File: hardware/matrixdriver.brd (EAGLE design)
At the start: 50 x 50 mm, 35 parts, among them IC1 75176AD, IC2 4017D, IC3 ULN2803, IC4 7805DT, Q1 20MHZ, Q2 MMBT4403LT1SMD, Q3 MMBT4403LT1SMD, Q4 MMBT4403LT1SMD, Q5 MMBT4403LT1SMD, Q6 MMBT4403LT1SMD, Q7 MMBT4403LT1SMD, Q8 MMBT4403LT1SMD, Q9 MMBT4403LT1SMD

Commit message: Release Candidate
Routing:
- net N$16: track 41.9 -> 43.3 mm
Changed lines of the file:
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@@
 <grid distance="12.5" unitdist="mil" unit="mm" style="lines" multiple="25" display="no" altdistance="25" altunitdist="mil" altunit="mm"/>
 <layers>
-<layer number="1" name="Top" color="4" fill="1" visible="no" active="yes"/>
-<layer number="16" name="Bottom" color="1" fill="1" visible="no" active="yes"/>
+<layer number="1" name="Top" color="4" fill="1" visible="yes" active="yes"/>
+<layer number="16" name="Bottom" color="1" fill="1" visible="yes" active="yes"/>
 <layer number="17" name="Pads" color="2" fill="1" visible="yes" active="yes"/>
 <layer number="18" name="Vias" color="2" fill="1" visible="yes" active="yes"/>
 <layer number="19" name="Unrouted" color="6" fill="1" visible="yes" active="yes"/>
-<layer number="20" name="Dimension" color="15" fill="1" visible="no" active="yes"/>
+<layer number="20" name="Dimension" color="15" fill="1" visible="yes" active="yes"/>
 <layer number="21" name="tPlace" color="7" fill="1" visible="no" active="yes"/>
-<layer number="22" name="bPlace" color="7" fill="1" visible="yes" active="yes"/>
+<layer number="22" name="bPlace" color="7" fill="1" visible="no" active="yes"/>
 <layer number="23" name="tOrigins" color="15" fill="1" visible="yes" active="yes"/>
 <layer number="24" name="bOrigins" color="15" fill="1" visible="yes" active="yes"/>
 <layer number="25" name="tNames" color="7" fill="1" visible="yes" active="yes"/>
-<layer number="26" name="bNames" color="7" fill="1" visible="yes" active="yes"/>
-<layer number="27" name="tValues" color="7" fill="1" visible="yes" active="yes"/>
+<layer number="26" name="bNames" color="7" fill="1" visible="no" active="yes"/>
+<layer number="27" name="tValues" color="7" fill="1" visible="no" active="yes"/>
 <layer number="28" name="bValues" color="7" fill="1" visible="no" active="yes"/>
 <layer number="29" name="tStop" color="7" fill="3" visible="yes" active="yes"/>
@@
 <layer number="33" name="tFinish" color="6" fill="3" visible="yes" active="yes"/>
 <layer number="34" name="bFinish" color="6" fill="6" visible="yes" active="yes"/>
-<layer number="35" name="tGlue" color="7" fill="4" visible="no" active="yes"/>
-<layer number="36" name="bGlue" color="7" fill="5" visible="no" active="yes"/>
+<layer number="35" name="tGlue" color="7" fill="4" visible="yes" active="yes"/>
+<layer number="36" name="bGlue" color="7" fill="5" visible="yes" active="yes"/>
 <layer number="37" name="tTest" color="7" fill="1" visible="yes" active="yes"/>
 <layer number="38" name="bTest" color="7" fill="1" visible="yes" active="yes"/>
@@
 <layer number="98" name="Guide" color="6" fill="1" visible="no" active="no"/>
 <layer number="100" name="Muster" color="7" fill="1" visible="no" active="no"/>
-<layer number="101" name="Patch_Top" color="12" fill="4" visible="yes" active="yes"/>
+<layer number="101" name="Patch_Top" color="12" fill="4" visible="no" active="yes"/>
 <layer number="102" name="Vscore" color="7" fill="1" visible="no" active="yes"/>
 <layer number="103" name="fp3" color="7" fill="1" visible="no" active="yes"/>
-<layer number="104" name="Name" color="7" fill="1" visible="yes" active="yes"/>
+<layer number="104" name="Name" color="7" fill="1" visible="no" active="yes"/>
 <layer number="105" name="Beschreib" color="9" fill="1" visible="no" active="yes"/>
-<layer number="106" name="BGA-Top" color="4" fill="1" visible="yes" active="yes"/>
-<layer number="107" name="BD-Top" color="5" fill="1" visible="yes" active="yes"/>
+<layer number="106" name="BGA-Top" color="4" fill="1" visible="no" active="yes"/>
+<layer number="107" name="BD-Top" color="5" fill="1" visible="no" active="yes"/>
 <layer number="108" name="fp8" color="7" fill="1" visible="no" active="yes"/>
 <layer number="109" name="fp9" color="7" fill="1" visible="no" active="yes"/>
@@
 <layer number="111" name="LPC17xx" color="7" fill="1" visible="yes" active="yes"/>
 <layer number="112" name="tSilk" color="7" fill="1" visible="yes" active="yes"/>
-<layer number="116" name="Patch_BOT" color="9" fill="4" visible="yes" active="yes"/>
+<layer number="116" name="Patch_BOT" color="9" fill="4" visible="no" active="yes"/>
 <layer number="121" name="_tsilk" color="7" fill="1" visible="yes" active="yes"/>
 <layer number="122" name="_bsilk" color="7" fill="1" visible="yes" active="yes"/>
@@
 <wire x1="50" y1="50" x2="0" y2="50" width="0" layer="20"/>
 <wire x1="0" y1="50" x2="0" y2="0" width="0" layer="20"/>
-<text x="2.2225" y="48.26" size="1.016" layer="1" font="vector" rot="R270">dirarare
+<text x="2.8575" y="46.355" size="1.016" layer="1" font="vector" rot="R270">dirarare
 Matrixdriver</text>
-<text x="46.6725" y="7.9375" size="1.016" layer="1" font="vector" rot="R270">REV 1</text>
-<hole x="2.5" y="48" drill="1.1"/>
-<hole x="48" y="2.5" drill="1.1"/>
-<hole x="48" y="48" drill="1.1"/>
+<text x="48.26" y="9.525" size="1.016" layer="1" font="vector" rot="R270">REV 1</text>
+<hole x="2.5" y="47.5" drill="1.1"/>
+<hole x="47.5" y="2.5" drill="1.1"/>
+<hole x="47.5" y="47.5" drill="1.1"/>
 <hole x="2.5" y="2.5" drill="1.1"/>
 </plain>
@@
 <contactref element="C4" pad="2"/>
 <contactref element="IC2" pad="8"/>
-<via x="5.715" y="39.37" extent="1-16" drill="0.6"/>
+<via x="6.6675" y="39.37" extent="1-16" drill="0.6"/>
 <via x="21.59" y="27.305" extent="1-16" drill="0.6"/>
 <via x="19.685" y="10.4775" extent="1-16" drill="0.6"/>
@@
 <vertex x="0.3175" y="0.9525"/>
 <vertex x="0.9525" y="0.3175"/>
-<vertex x="49.53" y="0.3175"/>
-<vertex x="49.2125" y="0.9525"/>
+<vertex x="49.8475" y="0.3175"/>
 <vertex x="49.8475" y="49.8475"/>
 </polygon>
@@
 <wire x1="33.02" y1="20.32" x2="33.655" y2="19.685" width="0.4064" layer="1"/>
 <via x="33.655" y="19.685" extent="1-16" drill="0.6"/>
-<wire x1="33.655" y1="19.685" x2="33.02" y2="20.32" width="0.4064" layer="16"/>
-<wire x1="33.02" y1="20.32" x2="22.225" y2="20.32" width="0.4064" layer="16"/>
-<wire x1="22.225" y1="20.32" x2="21.59" y2="20.955" width="0.4064" layer="16"/>
+<wire x1="33.655" y1="19.685" x2="33.02" y2="19.05" width="0.4064" layer="16"/>
+<wire x1="33.02" y1="19.05" x2="21.9075" y2="19.05" width="0.4064" layer="16"/>
+<wire x1="21.9075" y1="19.05" x2="21.59" y2="19.3675" width="0.4064" layer="16"/>
+<wire x1="21.59" y1="19.3675" x2="21.59" y2="20.955" width="0.4064" layer="16"/>
 <via x="21.59" y="20.955" extent="1-16" drill="0.6" shape="octagon"/>
 <wire x1="21.59" y1="20.955" x2="21.59" y2="19.05" width="0.4064" layer="1"/>

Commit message: REV.1 Finalisation
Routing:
- net N$65: vias 1 -> 2
- net N$62: vias 0 -> 1
- net N$61: vias 0 -> 1
- net N$60: vias 2 -> 1
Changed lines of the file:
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@@
 <via x="24.13" y="36.195" extent="1-16" drill="0.6"/>
 <via x="35.56" y="24.13" extent="1-16" drill="0.6"/>
-<via x="19.05" y="20.955" extent="1-16" drill="0.6" shape="octagon"/>
+<via x="19.05" y="20.955" extent="1-16" drill="0.6"/>
 <contactref element="C5" pad="1"/>
 <via x="3.81" y="25.4" extent="1-16" drill="0.6"/>
@@
 <wire x1="21.9075" y1="19.05" x2="21.59" y2="19.3675" width="0.4064" layer="16"/>
 <wire x1="21.59" y1="19.3675" x2="21.59" y2="20.955" width="0.4064" layer="16"/>
-<via x="21.59" y="20.955" extent="1-16" drill="0.6" shape="octagon"/>
+<via x="21.59" y="20.955" extent="1-16" drill="0.6"/>
 <wire x1="21.59" y1="20.955" x2="21.59" y2="19.05" width="0.4064" layer="1"/>
 <wire x1="21.59" y1="19.05" x2="21.59" y2="18.5166" width="0.4064" layer="1"/>
@@
 <contactref element="JP4" pad="2"/>
 <contactref element="U$1" pad="6"/>
-<wire x1="22.225" y1="13.335" x2="19.685" y2="13.335" width="0.4064" layer="1"/>
-<via x="19.685" y="13.335" extent="1-16" drill="0.6" shape="octagon"/>
-<wire x1="19.685" y1="13.335" x2="12.065" y2="13.335" width="0.4064" layer="16"/>
+<wire x1="22.225" y1="13.335" x2="12.065" y2="13.335" width="0.4064" layer="16"/>
 <via x="12.065" y="13.335" extent="1-16" drill="0.6"/>
 <wire x1="12.065" y1="13.335" x2="12.065" y2="11.2395" width="0.4064" layer="1"/>
@@
 <contactref element="JP4" pad="4"/>
 <contactref element="U$1" pad="9"/>
-<wire x1="24.765" y1="13.335" x2="24.765" y2="14.605" width="0.4064" layer="1"/>
-<wire x1="24.765" y1="14.605" x2="24.13" y2="15.24" width="0.4064" layer="1"/>
-<wire x1="24.13" y1="15.24" x2="16.51" y2="15.24" width="0.4064" layer="1"/>
+<wire x1="24.765" y1="13.335" x2="24.765" y2="14.605" width="0.4064" layer="16"/>
+<wire x1="24.765" y1="14.605" x2="24.13" y2="15.24" width="0.4064" layer="16"/>
+<wire x1="24.13" y1="15.24" x2="16.51" y2="15.24" width="0.4064" layer="16"/>
 <wire x1="16.51" y1="15.24" x2="15.875" y2="14.605" width="0.4064" layer="1"/>
 <wire x1="15.875" y1="14.605" x2="15.875" y2="11.2395" width="0.4064" layer="1"/>
+<via x="16.51" y="15.24" extent="1-16" drill="0.6"/>
 </signal>
 <signal name="N$62">
 <contactref element="JP4" pad="6"/>
 <contactref element="U$1" pad="11"/>
-<wire x1="27.305" y1="13.335" x2="27.305" y2="15.24" width="0.4064" layer="1"/>
+<wire x1="27.305" y1="13.335" x2="27.305" y2="15.24" width="0.4064" layer="16"/>
 <wire x1="27.305" y1="15.24" x2="26.67" y2="15.875" width="0.4064" layer="1"/>
 <wire x1="26.67" y1="15.875" x2="18.415" y2="15.875" width="0.4064" layer="1"/>
 <wire x1="18.415" y1="15.875" x2="17.145" y2="16.51" width="0.4064" layer="1"/>
 <wire x1="17.145" y1="16.51" x2="17.145" y2="20.4851" width="0.4064" layer="1"/>
+<via x="27.305" y="15.24" extent="1-16" drill="0.6"/>
 </signal>
 <signal name="N$65">
@@
 <contactref element="U$2" pad="+"/>
 <wire x1="40.18" y1="24.765" x2="40.005" y2="27.94" width="0.4064" layer="16"/>
-<via x="40.005" y="27.94" extent="1-16" drill="0.6" shape="square"/>
+<via x="40.005" y="27.94" extent="1-16" drill="0.6"/>
 <wire x1="40.005" y1="27.94" x2="40.005" y2="28.575" width="0.4064" layer="1"/>
 <wire x1="40.005" y1="28.575" x2="42.545" y2="31.115" width="0.4064" layer="1"/>
 <wire x1="42.545" y1="31.115" x2="42.545" y2="31.75" width="0.4064" layer="1"/>
 <wire x1="42.545" y1="31.75" x2="42.8625" y2="32.0675" width="0.4064" layer="1"/>
-<wire x1="41.91" y1="23.035" x2="40.18" y2="24.765" width="0.4064" layer="1"/>
+<wire x1="41.91" y1="23.035" x2="40.18" y2="24.765" width="0.4064" layer="16"/>
 <wire x1="44.075" y1="32.03" x2="42.9" y2="32.03" width="0.4064" layer="1"/>
 <wire x1="42.9" y1="32.03" x2="42.8625" y2="32.0675" width="0.4064" layer="1"/>
+<via x="41.91" y="23.035" extent="1-16" drill="0.6"/>
 </signal>
 <signal name="N$11">

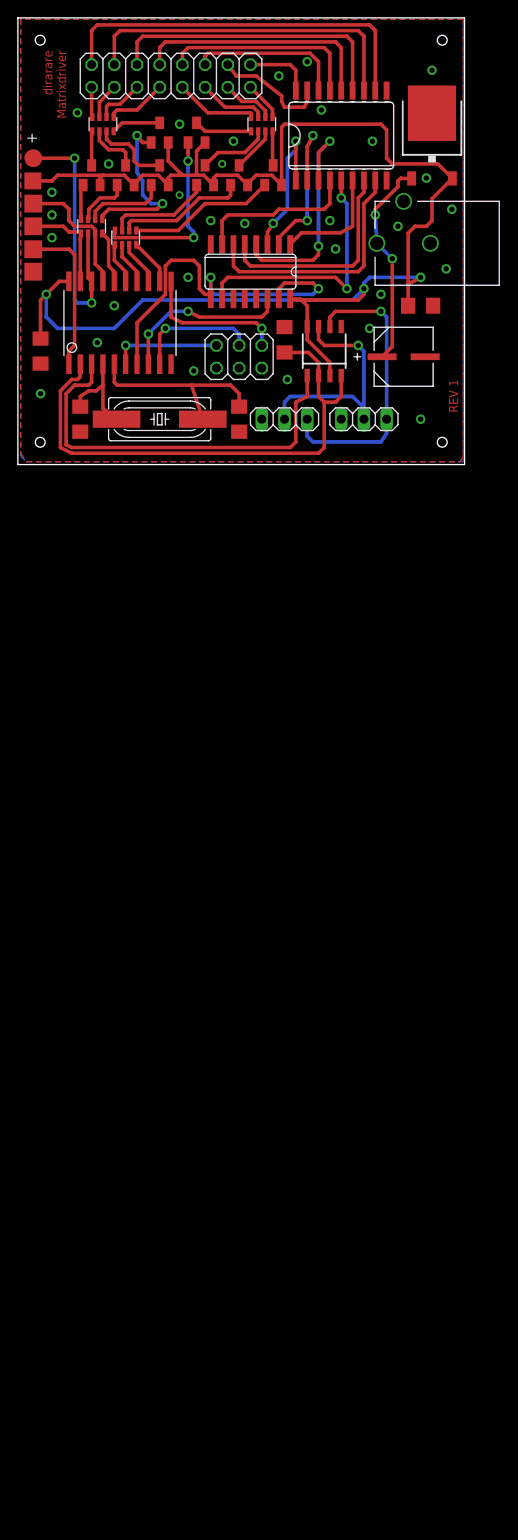
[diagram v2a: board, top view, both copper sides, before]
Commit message: Fix errors behind transistor
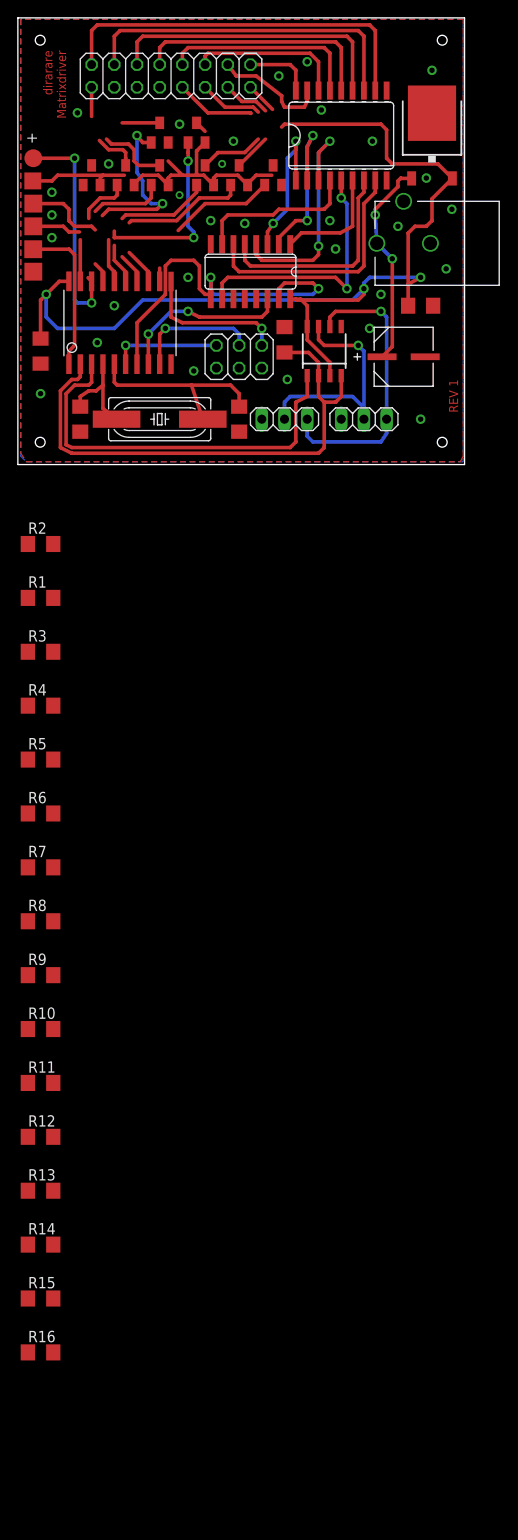
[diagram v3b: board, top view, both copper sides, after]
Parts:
- removed CTS742C083_1, CTS742C083_2: 1k, resistor-net:CTS742C083
- removed CTS742C083_3, CTS742C083_4: 10, resistor-net:CTS742C083
- added R1, R2, R3, R4, R5, R6, R7, R8: 1k, resistor:R1206
- added R10, R11, R12, R13, R14, R15, R16, R9: 10, resistor:R1206
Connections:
- removed net N$34: CTS742C083_3.7, JP1.3
- removed net N$35: CTS742C083_3.6, JP1.5
- removed net N$36: CTS742C083_3.5, JP1.7
- removed net N$56: CTS742C083_3.1, Q2.C
- new net N$44: Q2.E, R9.1
- new net N$45: Q3.E, R10.1
- new net N$46: Q5.E, R12.1
- new net N$461: C4.1, C5.2, IC1.3, IC1.8, IC2.16, IC4.2, Q4.E, Q6.E, Q7.E, Q8.E, R11.1, TP2.TP, U$1.20
- net N$1: now also R5.1; no longer CTS742C083_2.4
- net N$13: now also R16.2; no longer CTS742C083_4.8
- net N$2: now also R6.1; no longer CTS742C083_2.3
- net N$29: now also R15.2; no longer CTS742C083_4.7
- net N$3: now also R7.1; no longer CTS742C083_2.2
- net N$30: now also R14.2; no longer CTS742C083_4.6
- net N$31: now also R13.2; no longer CTS742C083_4.5
- net N$32: now also R3.2; no longer CTS742C083_1.7
- net N$33: now also Q2.C; no longer CTS742C083_3.8
- net N$37: now also R4.2; no longer CTS742C083_1.8
- net N$38: now also R2.2; no longer CTS742C083_1.6
- net N$39: now also R1.2; no longer CTS742C083_1.5
- net N$4: now also R8.1; no longer CTS742C083_2.1
- net N$40: now also R6.2; no longer CTS742C083_2.6
- net N$41: now also R5.2; no longer CTS742C083_2.5
- net N$42: now also R8.2; no longer CTS742C083_2.8
- net N$43: now also R7.2; no longer CTS742C083_2.7
- net N$49: now also R13.1; no longer CTS742C083_4.4
- net N$5: now also R1.1; no longer CTS742C083_1.4
- net N$50: now also R14.1; no longer CTS742C083_4.3
- net N$51: now also R15.1; no longer CTS742C083_4.2
- net N$52: now also R16.1; no longer CTS742C083_4.1
- net N$53: now also JP1.7; no longer CTS742C083_3.4
- net N$54: now also JP1.5; no longer CTS742C083_3.3
- net N$55: now also JP1.3; no longer CTS742C083_3.2
- net N$6: now also R2.1; no longer CTS742C083_1.3
- net N$7: now also R3.1; no longer CTS742C083_1.2
- net N$8: now also R4.1; no longer CTS742C083_1.1
- net VCC: now also R10.2, R12.2, R9.2; no longer C4.1, C5.2, IC1.3, IC1.8, IC2.16, IC4.2, Q2.E, Q3.E, Q4.E, Q5.E, Q6.E, Q7.E, Q8.E, Q9.E, TP2.TP, U$1.20
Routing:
- net VCC: track 167.4 -> 0.00 mm, vias 3 -> 0
- net N$461: track 0.00 -> 154.8 mm, vias 0 -> 3
- net N$36: track 6.76 -> 0.00 mm
- net N$35: track 5.48 -> 0.00 mm
- net N$52: track 6.49 -> 1.34 mm
- net N$7: track 30.5 -> 25.5 mm
- net N$41: track 16.5 -> 11.8 mm
- net N$34: track 4.02 -> 0.00 mm
- net N$56: track 3.84 -> 0.00 mm
- net N$6: track 15.0 -> 11.2 mm
- net N$49: track 3.84 -> 0.10 mm
- net N$1: track 5.17 -> 1.48 mm
- net N$37: track 3.92 -> 0.35 mm
- net N$43: track 11.9 -> 10.6 mm
- net N$3: track 4.78 -> 3.44 mm
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
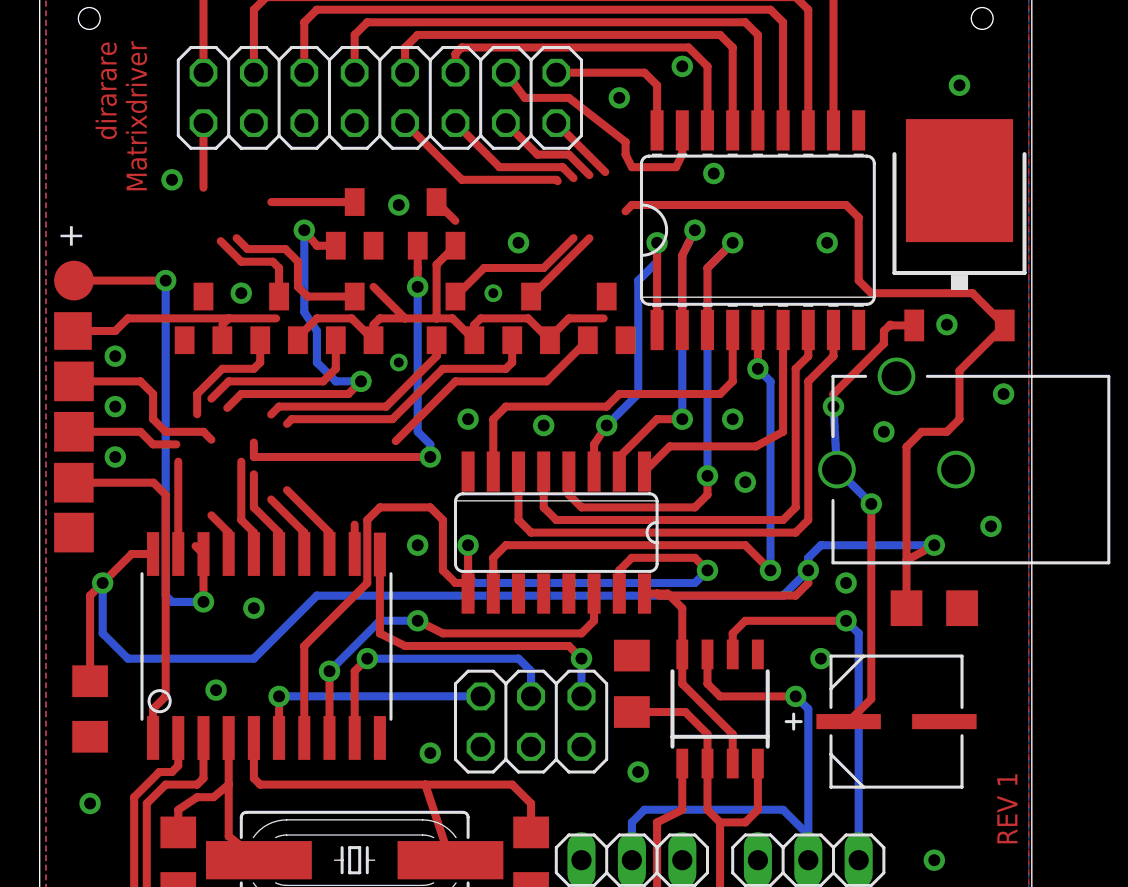
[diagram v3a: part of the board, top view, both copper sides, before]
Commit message: fix some errors in schema
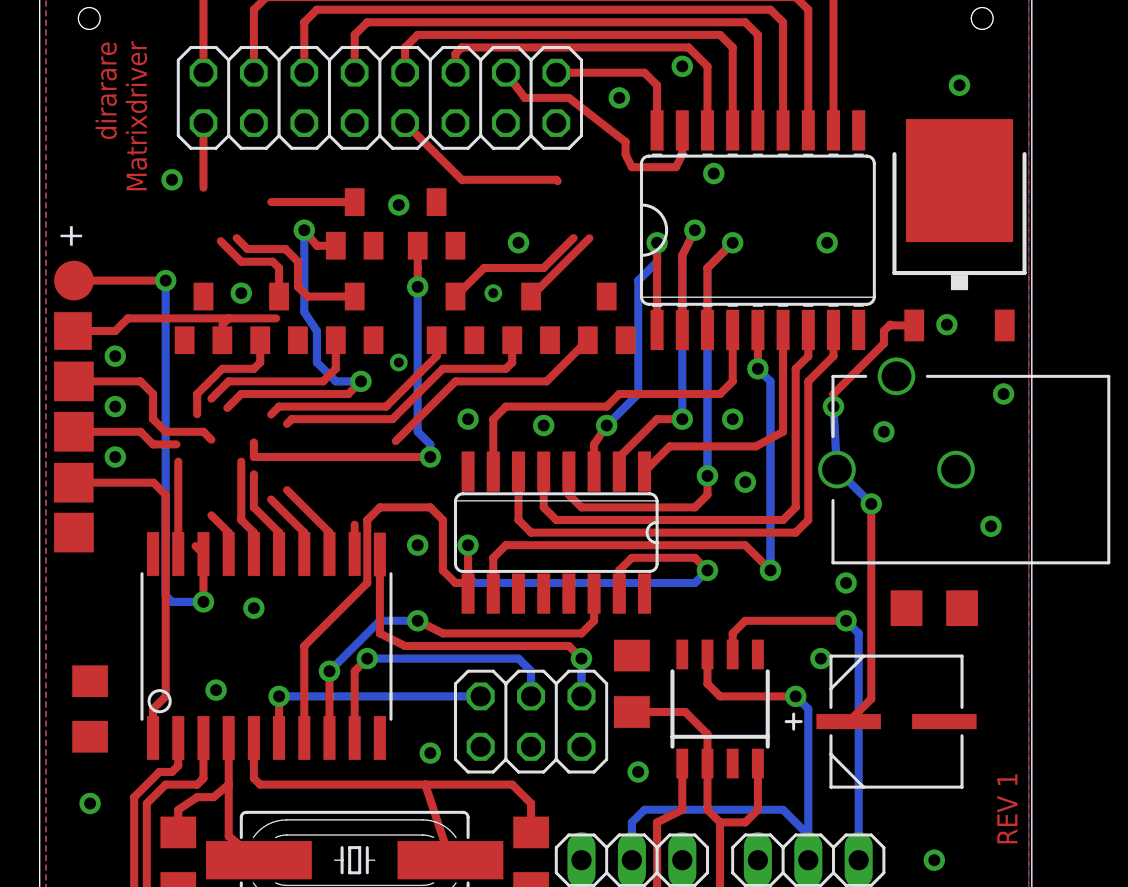
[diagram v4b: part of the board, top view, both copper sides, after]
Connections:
- removed net N$52: Q6.C, R16.1
- new net N$34: Q9.E, R13.1
- new net N$35: Q7.E, R15.1
- net N$13: now also Q6.C; no longer R16.2
- net N$29: now also Q8.E, R14.1; no longer JP1.11, R15.2
- net N$30: now also Q4.E, R11.1; no longer JP1.13, R14.2
- net N$31: now also Q6.E, R16.1; no longer JP1.15, R13.2
- net N$461: no longer C4.1, C5.2, IC1.3, IC1.8, IC2.16, IC4.2, Q4.E, Q6.E, Q7.E, Q8.E, R11.1, U$1.20
- net N$49: now also JP1.15; no longer R13.1
- net N$50: now also JP1.13; no longer R14.1
- net N$51: now also JP1.11; no longer R15.1
- net VCC: now also C4.1, C5.2, IC1.3, IC1.8, IC2.16, IC4.2, R11.2, R13.2, R14.2, R15.2, R16.2, U$1.20
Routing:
- net N$461: track 154.8 -> 11.0 mm, vias 3 -> 0
- net N$29: track 7.10 -> 0.00 mm
- net N$30: track 5.30 -> 0.00 mm
- net N$31: track 3.49 -> 0.00 mm
- net N$52: track 1.34 -> 0.00 mm
